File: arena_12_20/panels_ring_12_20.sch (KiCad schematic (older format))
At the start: 32 parts, among them J1 DB9, P1 COLUMN_0, P10 COLUMN_9, P11 COLUMN_10, P12 COLUMN_11, P13 DIN_5, P14 CONN_5X2, P15 CONN_2, P16 CONN_1, P17 CONN_1, P18 CONN_1, P19 CONN_1, P2 COLUMN_1, P20 CONN_1, P21 CONN_1, P22 CONN_1, P23 CONN_1, P24 CONN_1, P25 CONN_1, P26 CONN_1, P27 CONN_1, P28 CONN_1, P3 COLUMN_2, P4 COLUMN_3, P5 COLUMN_4, P6 COLUMN_5, P7 COLUMN_6, P8 COLUMN_7, P9 COLUMN_8, SW1 SWITCH_INV

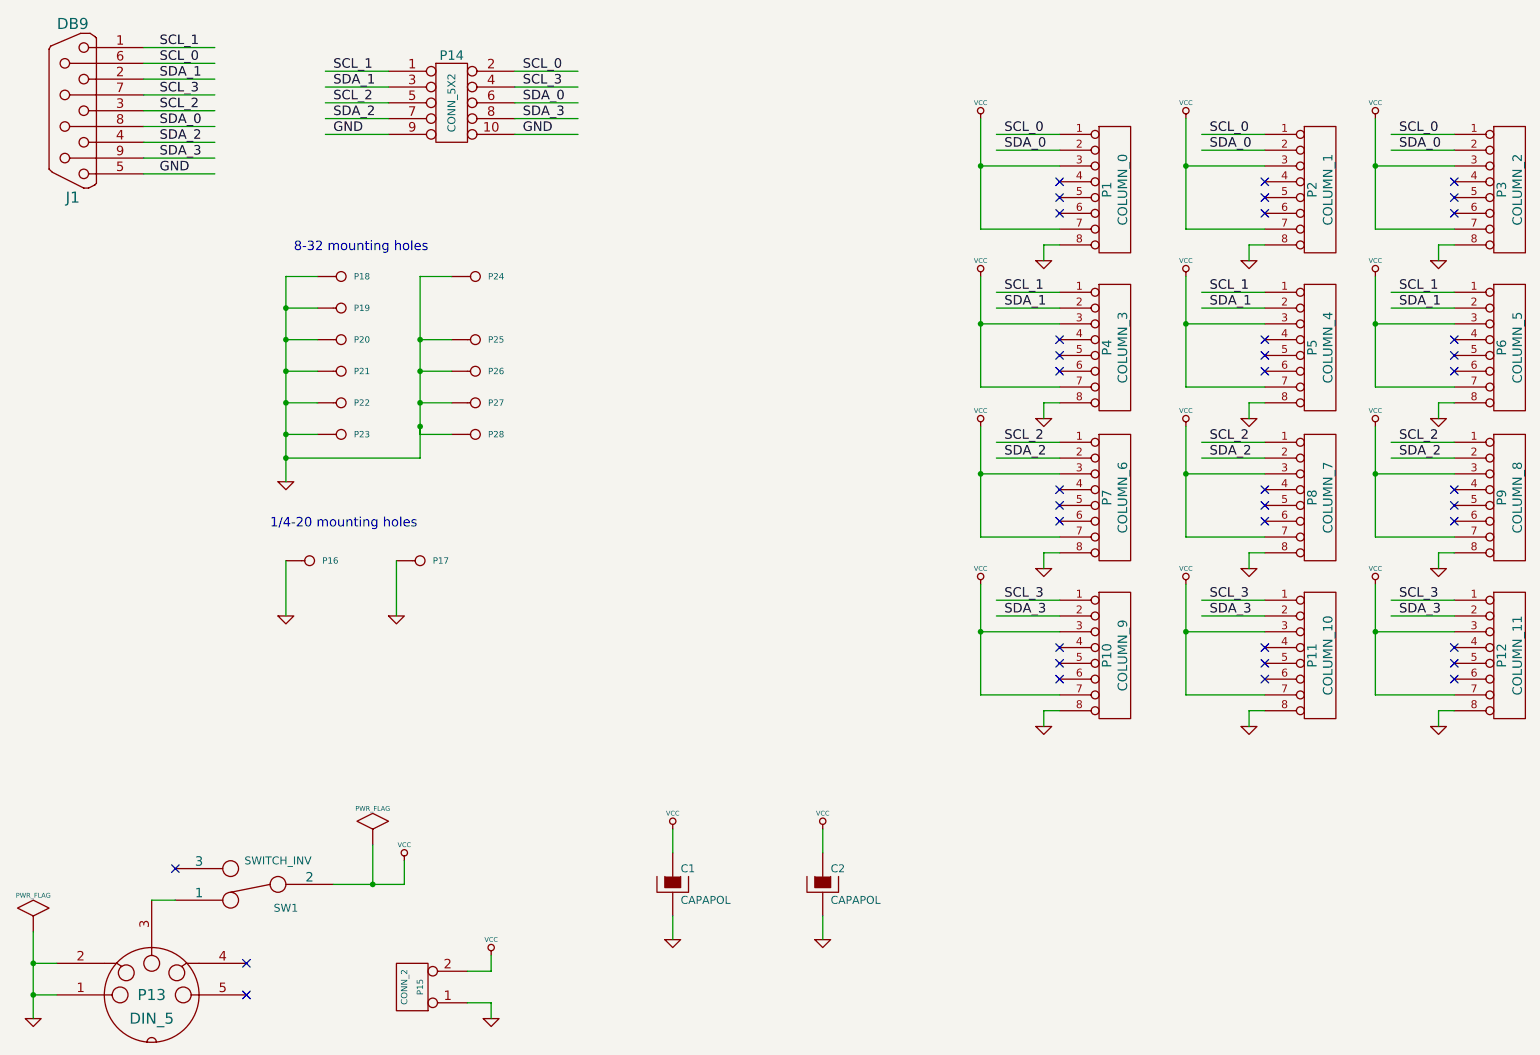
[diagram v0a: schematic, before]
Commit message: Version 2 redesign.  Increased arena radius so panels will fit.
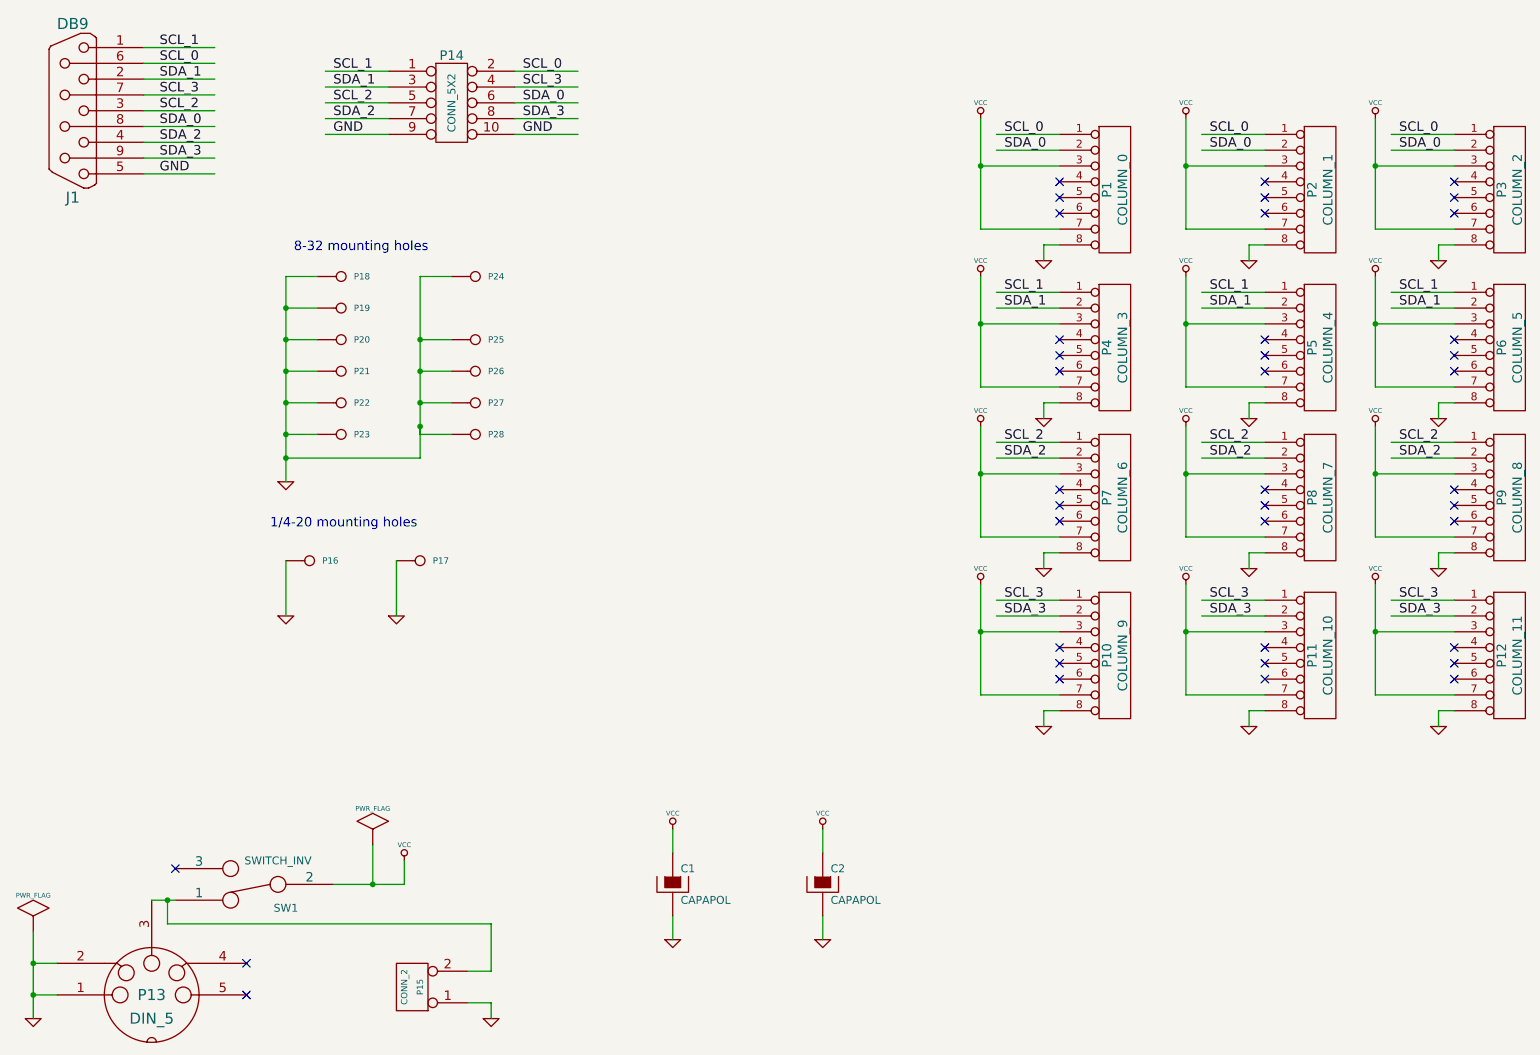
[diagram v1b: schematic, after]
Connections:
- wire segments 135 -> 137

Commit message: KiCAD cleanup
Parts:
- C1, C2: symbol CAPAPOL -> panels_ring_12_20-rescue:CAPAPOL
- J1: symbol DB9 -> panels_ring_12_20-rescue:DB9
- P1, P10, P11, P12, P2, P3, P4, P5, P6, P7, P8, P9: symbol CONN_8 -> panels_ring_12_20-rescue:CONN_8
- P13: symbol DIN_5 -> panels_ring_12_20-rescue:DIN_5
- P14: symbol CONN_5X2 -> panels_ring_12_20-rescue:CONN_5X2
- P15: symbol CONN_2 -> panels_ring_12_20-rescue:CONN_2
- P16, P17, P18, P19, P20, P21, P22, P23, P24, P25, P26, P27, P28: symbol CONN_1 -> panels_ring_12_20-rescue:CONN_1
- SW1: symbol SWITCH_INV -> panels_ring_12_20-rescue:SWITCH_INV
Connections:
- wire segments 137 -> 161

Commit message: more cleanup
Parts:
- C1, C2: symbol panels_ring_12_20-rescue:CAPAPOL -> panels_ring_12_20:CAPAPOL
- J1: symbol panels_ring_12_20-rescue:DB9 -> panels_ring_12_20:DB9
- P1, P10, P11, P12, P2, P3, P4, P5, P6, P7, P8, P9: symbol panels_ring_12_20-rescue:CONN_8 -> panels_ring_12_20:CONN_8
- P13: symbol panels_ring_12_20-rescue:DIN_5 -> panels_ring_12_20:DIN_5
- P14: symbol panels_ring_12_20-rescue:CONN_5X2 -> panels_ring_12_20:CONN_5X2
- P15: symbol panels_ring_12_20-rescue:CONN_2 -> panels_ring_12_20:CONN_2
- P16, P17, P18, P19, P20, P21, P22, P23, P24, P25, P26, P27, P28: symbol panels_ring_12_20-rescue:CONN_1 -> panels_ring_12_20:CONN_1
- SW1: symbol panels_ring_12_20-rescue:SWITCH_INV -> panels_ring_12_20:SWITCH_INV
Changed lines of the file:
@@
 	3900 3400 3700 3400
 $Comp
-L panels_ring_12_20-rescue:CONN_1 P28
+L panels_ring_12_20:CONN_1 P28
 U 1 1 4D19112A
 P 4050 3400
@@
 $EndComp
 $Comp
-L panels_ring_12_20-rescue:CONN_1 P27
+L panels_ring_12_20:CONN_1 P27
 U 1 1 4D191129
 P 4050 3200
@@
 $EndComp
 $Comp
-L panels_ring_12_20-rescue:CONN_1 P26
+L panels_ring_12_20:CONN_1 P26
 U 1 1 4D191126
 P 4050 3000
@@
 $EndComp
 $Comp
-L panels_ring_12_20-rescue:CONN_1 P25
+L panels_ring_12_20:CONN_1 P25
 U 1 1 4D191125
 P 4050 2800
@@
 $EndComp
 $Comp
-L panels_ring_12_20-rescue:CONN_1 P24
+L panels_ring_12_20:CONN_1 P24
 U 1 1 4D19111C
 P 4050 2400
@@
 8-32 mounting holes
 $Comp
-L panels_ring_12_20-rescue:GND #PWR01
+L panels_ring_12_20:GND #PWR01
 U 1 1 4D19062B
 P 2850 3700
@@
 $EndComp
 $Comp
-L panels_ring_12_20-rescue:CONN_1 P23
+L panels_ring_12_20:CONN_1 P23
 U 1 1 4D1905C4
 P 3200 3400
@@
 $EndComp
 $Comp
-L panels_ring_12_20-rescue:CONN_1 P20
+L panels_ring_12_20:CONN_1 P20
 U 1 1 4D1905C2
 P 3200 2800
@@
 $EndComp
 $Comp
-L panels_ring_12_20-rescue:CONN_1 P19
+L panels_ring_12_20:CONN_1 P19
 U 1 1 4D1905C0
 P 3200 2600
@@
 $EndComp
 $Comp
-L panels_ring_12_20-rescue:CONN_1 P18
+L panels_ring_12_20:CONN_1 P18
 U 1 1 4D1905BE
 P 3200 2400
@@
 $EndComp
 $Comp
-L panels_ring_12_20-rescue:CONN_1 P22
+L panels_ring_12_20:CONN_1 P22
 U 1 1 4D1905BC
 P 3200 3200
@@
 $EndComp
 $Comp
-L panels_ring_12_20-rescue:CONN_1 P21
+L panels_ring_12_20:CONN_1 P21
 U 1 1 4D1905B4
 P 3200 3000
@@
 NoConn ~ 2150 6150
 $Comp
-L panels_ring_12_20-rescue:SWITCH_INV SW1
+L panels_ring_12_20:SWITCH_INV SW1
 U 1 1 4D13B1B5
 P 2650 6250
@@
 $EndComp
 $Comp
-L panels_ring_12_20-rescue:CONN_1 P17
+L panels_ring_12_20:CONN_1 P17
 U 1 1 4D13AE2D
 P 3700 4200
@@
 $EndComp
 $Comp
-L panels_ring_12_20-rescue:CONN_1 P16
+L panels_ring_12_20:CONN_1 P16
 U 1 1 4D13AE27
 P 3000 4200
@@
 $EndComp
 $Comp
-L panels_ring_12_20-rescue:GND #PWR04
+L panels_ring_12_20:GND #PWR04
 U 1 1 4D12B446
 P 4150 7100
@@
 $EndComp
 $Comp
-L panels_ring_12_20-rescue:CONN_2 P15
+L panels_ring_12_20:CONN_2 P15
 U 1 1 4D12B40B
 P 3650 6900
@@
 SCL_1
 $Comp
-L panels_ring_12_20-rescue:CONN_5X2 P14
+L panels_ring_12_20:CONN_5X2 P14
 U 1 1 4D12B1EB
 P 3900 1300
@@
 $EndComp
 $Comp
-L panels_ring_12_20-rescue:GND #PWR06
+L panels_ring_12_20:GND #PWR06
 U 1 1 4D12AF2A
 P 3550 4550
@@
 $EndComp
 $Comp
-L panels_ring_12_20-rescue:GND #PWR07
+L panels_ring_12_20:GND #PWR07
 U 1 1 4D12AF26
 P 2850 4550
@@
 $EndComp
 $Comp
-L panels_ring_12_20-rescue:VCC #PWR08
+L panels_ring_12_20:VCC #PWR08
 U 1 1 4D12AC6C
 P 9750 4350
@@
 $EndComp
 $Comp
-L panels_ring_12_20-rescue:VCC #PWR09
+L panels_ring_12_20:VCC #PWR09
 U 1 1 4D12AC67
 P 8550 4350
@@
 $EndComp
 $Comp
-L panels_ring_12_20-rescue:VCC #PWR010
+L panels_ring_12_20:VCC #PWR010
 U 1 1 4D12AC62
 P 7250 4350
@@
 $EndComp
 $Comp
-L panels_ring_12_20-rescue:VCC #PWR011
+L panels_ring_12_20:VCC #PWR011
 U 1 1 4D12AC5C
 P 9750 3350
@@
 $EndComp
 $Comp
-L panels_ring_12_20-rescue:VCC #PWR012
+L panels_ring_12_20:VCC #PWR012
 U 1 1 4D12AC58
 P 8550 3350
@@
 $EndComp
 $Comp
-L panels_ring_12_20-rescue:VCC #PWR013
+L panels_ring_12_20:VCC #PWR013
 U 1 1 4D12AC53
 P 7250 3350
@@
 $EndComp
 $Comp
-L panels_ring_12_20-rescue:VCC #PWR014
+L panels_ring_12_20:VCC #PWR014
 U 1 1 4D12AC4D
 P 9750 2400
@@
 $EndComp
 $Comp
-L panels_ring_12_20-rescue:VCC #PWR015
+L panels_ring_12_20:VCC #PWR015
 U 1 1 4D12AC47
 P 8550 2400
@@
 $EndComp
 $Comp
-L panels_ring_12_20-rescue:VCC #PWR016
+L panels_ring_12_20:VCC #PWR016
 U 1 1 4D12AC42
 P 7250 2400
@@
 $EndComp
 $Comp
-L panels_ring_12_20-rescue:VCC #PWR017
+L panels_ring_12_20:VCC #PWR017
 U 1 1 4D12AC3D
 P 9750 1400
@@
 $EndComp
 $Comp
-L panels_ring_12_20-rescue:VCC #PWR018
+L panels_ring_12_20:VCC #PWR018
 U 1 1 4D12AC37
 P 8550 1400
@@
 $EndComp
 $Comp
-L panels_ring_12_20-rescue:VCC #PWR019
+L panels_ring_12_20:VCC #PWR019
 U 1 1 4D12AC18
 P 7250 1400
@@
 SCL_0
 $Comp
-L panels_ring_12_20-rescue:GND #PWR020
+L panels_ring_12_20:GND #PWR020
 U 1 1 4D12A99C
 P 10150 5250
@@
 $EndComp
 $Comp
-L panels_ring_12_20-rescue:GND #PWR021
+L panels_ring_12_20:GND #PWR021
 U 1 1 4D12A997
 P 8950 5250
@@
 $EndComp
 $Comp
-L panels_ring_12_20-rescue:GND #PWR022
+L panels_ring_12_20:GND #PWR022
 U 1 1 4D12A993
 P 7650 5250
@@
 $EndComp
 $Comp
-L panels_ring_12_20-rescue:GND #PWR023
+L panels_ring_12_20:GND #PWR023
 U 1 1 4D12A98C
 P 10150 4250
@@
 $EndComp
 $Comp
-L panels_ring_12_20-rescue:GND #PWR024
+L panels_ring_12_20:GND #PWR024
 U 1 1 4D12A989
 P 8950 4250
@@
 $EndComp
 $Comp
-L panels_ring_12_20-rescue:GND #PWR025
+L panels_ring_12_20:GND #PWR025
 U 1 1 4D12A983
 P 7650 4250
@@
 $EndComp
 $Comp
-L panels_ring_12_20-rescue:GND #PWR026
+L panels_ring_12_20:GND #PWR026
 U 1 1 4D12A97B
 P 10150 3300
@@
 $EndComp
 $Comp
-L panels_ring_12_20-rescue:GND #PWR027
+L panels_ring_12_20:GND #PWR027
 U 1 1 4D12A973
 P 8950 3300
@@
 $EndComp
 $Comp
-L panels_ring_12_20-rescue:GND #PWR028
+L panels_ring_12_20:GND #PWR028
 U 1 1 4D12A96D
 P 7650 3300
@@
 $EndComp
 $Comp
-L panels_ring_12_20-rescue:GND #PWR029
+L panels_ring_12_20:GND #PWR029
 U 1 1 4D12A95F
 P 10150 2300
@@
 $EndComp
 $Comp
-L panels_ring_12_20-rescue:GND #PWR030
+L panels_ring_12_20:GND #PWR030
 U 1 1 4D12A950
 P 8950 2300
@@
 $EndComp
 $Comp
-L panels_ring_12_20-rescue:GND #PWR031
+L panels_ring_12_20:GND #PWR031
 U 1 1 4D12A94E
 P 7650 2300
@@
 NoConn ~ 7750 1800
 $Comp
-L panels_ring_12_20-rescue:GND #PWR032
+L panels_ring_12_20:GND #PWR032
 U 1 1 4D12A6CB
 P 6250 6600
@@
 $EndComp
 $Comp
-L panels_ring_12_20-rescue:GND #PWR033
+L panels_ring_12_20:GND #PWR033
 U 1 1 4D12A6C8
 P 5300 6600
@@
 $EndComp
 $Comp
-L panels_ring_12_20-rescue:VCC #PWR034
+L panels_ring_12_20:VCC #PWR034
 U 1 1 4D12A6C1
 P 6250 5900
@@
 $EndComp
 $Comp
-L panels_ring_12_20-rescue:VCC #PWR035
+L panels_ring_12_20:VCC #PWR035
 U 1 1 4D12A6BC
 P 5300 5900
@@
 $EndComp
 $Comp
-L panels_ring_12_20-rescue:VCC #PWR036
+L panels_ring_12_20:VCC #PWR036
 U 1 1 4D12A0AF
 P 3600 6100
@@
 $EndComp
 $Comp
-L panels_ring_12_20-rescue:GND #PWR037
+L panels_ring_12_20:GND #PWR037
 U 1 1 4D12A09E
 P 1250 7100
@@
 SCL_1
 $Comp
-L panels_ring_12_20-rescue:CAPAPOL C2
+L panels_ring_12_20:CAPAPOL C2
 U 1 1 4D129B77
 P 6250 6250
@@
 $EndComp
 $Comp
-L panels_ring_12_20-rescue:CAPAPOL C1
+L panels_ring_12_20:CAPAPOL C1
 U 1 1 4D129B16
 P 5300 6250
@@
 $EndComp
 $Comp
-L panels_ring_12_20-rescue:DIN_5 P13
+L panels_ring_12_20:DIN_5 P13
 U 1 1 4D129A69
 P 2000 6950
@@
 $EndComp
 $Comp
-L panels_ring_12_20-rescue:DB9 J1
+L panels_ring_12_20:DB9 J1
 U 1 1 4D1299C1
 P 1500 1350
@@
 $EndComp
 $Comp
-L panels_ring_12_20-rescue:CONN_8 P3
+L panels_ring_12_20:CONN_8 P3
 U 1 1 4D1299A0
 P 10600 1850
@@
 $EndComp
 $Comp
-L panels_ring_12_20-rescue:CONN_8 P6
+L panels_ring_12_20:CONN_8 P6
 U 1 1 4D12999F
 P 10600 2850
@@
 $EndComp
 $Comp
-L panels_ring_12_20-rescue:CONN_8 P12
+L panels_ring_12_20:CONN_8 P12
 U 1 1 4D12999E
 P 10600 4800
@@
 $EndComp
 $Comp
-L panels_ring_12_20-rescue:CONN_8 P9
+L panels_ring_12_20:CONN_8 P9
 U 1 1 4D12999D
 P 10600 3800
@@
 $EndComp
 $Comp
-L panels_ring_12_20-rescue:CONN_8 P8
+L panels_ring_12_20:CONN_8 P8
 U 1 1 4D129997
 P 9400 3800
@@
 $EndComp
 $Comp
-L panels_ring_12_20-rescue:CONN_8 P11
+L panels_ring_12_20:CONN_8 P11
 U 1 1 4D129996
 P 9400 4800
@@
 $EndComp
 $Comp
-L panels_ring_12_20-rescue:CONN_8 P5
+L panels_ring_12_20:CONN_8 P5
 U 1 1 4D129995
 P 9400 2850
@@
 $EndComp
 $Comp
-L panels_ring_12_20-rescue:CONN_8 P2
+L panels_ring_12_20:CONN_8 P2
 U 1 1 4D129994
 P 9400 1850
@@
 $EndComp
 $Comp
-L panels_ring_12_20-rescue:CONN_8 P1
+L panels_ring_12_20:CONN_8 P1
 U 1 1 4D12997C
 P 8100 1850
@@
 $EndComp
 $Comp
-L panels_ring_12_20-rescue:CONN_8 P4
+L panels_ring_12_20:CONN_8 P4
 U 1 1 4D12997B
 P 8100 2850
@@
 $EndComp
 $Comp
-L panels_ring_12_20-rescue:CONN_8 P10
+L panels_ring_12_20:CONN_8 P10
 U 1 1 4D12996A
 P 8100 4800
@@
 $EndComp
 $Comp
-L panels_ring_12_20-rescue:CONN_8 P7
+L panels_ring_12_20:CONN_8 P7
 U 1 1 4D12995D
 P 8100 3800
